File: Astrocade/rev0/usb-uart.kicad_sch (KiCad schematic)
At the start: 13 parts, among them J3 USB-C, U3 CP2102N-A02-GQFN28, U4 UMH3N

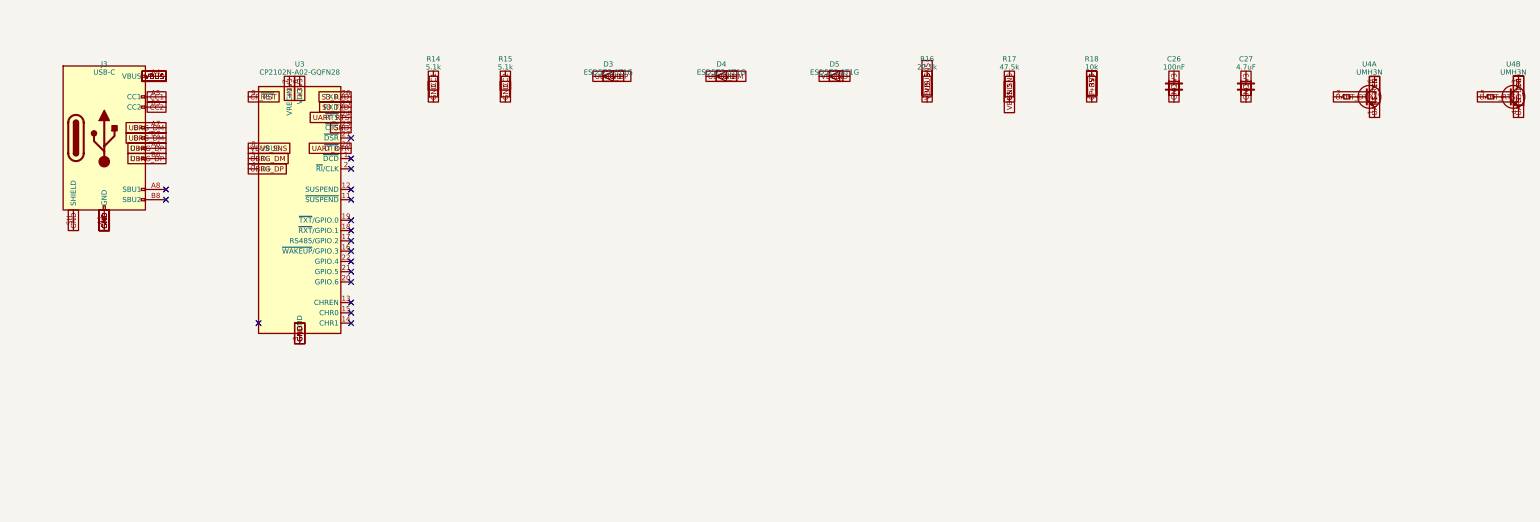
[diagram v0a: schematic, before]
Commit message: Astrocade Rev0: redo on RP2354A + ESP32-S3, 6-layer, fully autorouted
Replaces the unrouted RP2040 + 3x LVC245 draft with an INTV-style board:
RP2354A straight on the 5V bus, ESP32-S3-WROOM-1-N16R8 as its USB host
(PICOBOOT reflash), USB-C/CP2102N, push-push microSD, WS2812B-2020-V6,
RESET/BOOTSEL/EN/BOOT buttons. Same cassette outline, lands and holes.

Everything is generated by tools/ (build_all.sh): design.py -> schematic,
placement + plane fan-out, Raspberry Pi's MIT regulator-corner graft,
Freerouting + A* finisher, netlist-vs-firmware check, JLCPCB BOM/CPL/gerbers.
ERC 0, DRC 0 errors / 0 unconnected / 0 parity, check_nets 174/174.

RUN/BOOTSEL from the S3 are direct 1k links (fnPicoUpdater drives them low;
an NPN driver would invert it). Shell openings come from the placement.

Co-Authored-By: Claude Opus 5.5 (1M context) <noreply@anthropic.com>
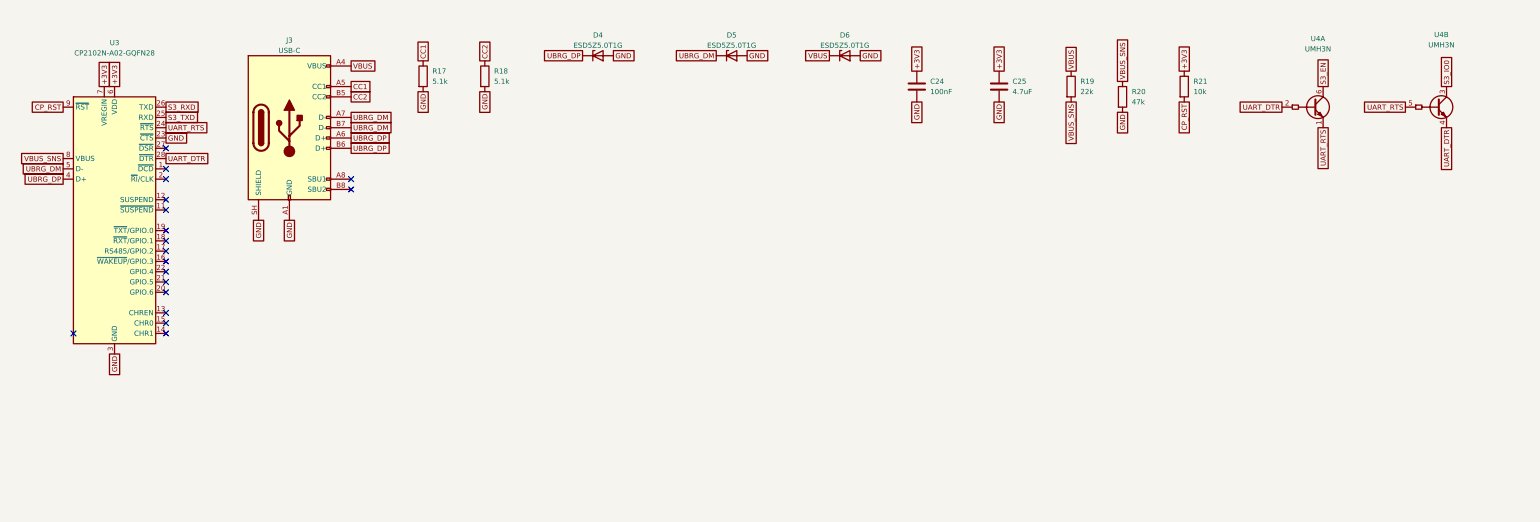
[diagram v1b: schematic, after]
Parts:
- removed C26: 100nF, FujiNet-Astrocade:C_0603_1608Metric, symbol Device:C
- removed C27: 4.7uF, FujiNet-Astrocade:C_0603_1608Metric, symbol Device:C
- removed D3: ESD5Z5.0T1G, FujiNet-Astrocade:D_SOD-523, symbol Diode:ESD5Zxx
- removed R14, R15: 5.1k, FujiNet-Astrocade:R_0603_1608Metric, symbol Device:R
- removed R16: 22.1k, FujiNet-Astrocade:R_0603_1608Metric, symbol Device:R
- added C24: 100nF, FujiNet-Astrocade:C_0603_1608Metric, symbol Device:C
- added C25: 4.7uF, FujiNet-Astrocade:C_0603_1608Metric, symbol Device:C
- added D6: ESD5Z5.0T1G, FujiNet-Astrocade:D_SOD-523, symbol Diode:ESD5Zxx
- added R19: 22k, FujiNet-Astrocade:R_0603_1608Metric, symbol Device:R
- added R20: 47k, FujiNet-Astrocade:R_0603_1608Metric, symbol Device:R
- added R21: 10k, FujiNet-Astrocade:R_0603_1608Metric, symbol Device:R
- D4, D5: LCSC C316061 -> C82044; MPN (none) -> ESD5Z5.0T1G
- J3: LCSC C5178539 -> C165948; MPN HRO TYPE-C-31-M-12 -> TYPE-C-31-M-12
- R17: value 47.5k -> 5.1k; LCSC (none) -> C23186; MPN (none) -> 0603WAF5101T5E
- R18: value 10k -> 5.1k; LCSC (none) -> C23186; MPN (none) -> 0603WAF5101T5E
- U3: LCSC (none) -> C964632
- U4: LCSC C123008 -> C62892; MPN (none) -> UMH3N
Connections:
- net +3V3: now also C24.1, C25.1, R21.1; no longer R18.1
- net CC1: now also R17.1
- net CC2: now also R18.1
- net CP_RST: now also R21.2; no longer R18.2
- net GND: now also R18.2, C24.2, C25.2, D6.2 (A), R20.2
- net UBRG_DM: now also D5.1 (K); no longer D4.1 (K)
- net UBRG_DP: now also D4.1 (K)
- net VBUS: now also D6.1 (K), R19.1; no longer D5.1 (K)
- net VBUS_SNS: now also R19.2, R20.1; no longer R17.1
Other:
- company: (none) -> FujiNet
- title: (none) -> FujiNet Astrocade Rev0 - USB-C, CP2102N programming bridge

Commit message: Astrocade Rev0: audit with kicad-happy + datasheets and redo
Schematic, board and fab outputs regenerated from tools/ after a
datasheet-level audit (docs/design-review-rev0.md).

Design fixes:
- RP2354A on its own AP2112K rail (+3V3_RP): its FT pads take 5.5 V only
  with IOVDD powered (RP2350 DS p.1332); the buck's UVLO + 4 ms soft-start
  left them unpowered while the console drove the bus
- WS2812B-2020-V6 on +5V (datasheet VDD 3.7-5.3 V, not a 3.3 V part)
- VBUS decoupling at the USB-C, activity LED 330R, card-detect polarity
  settled (low = card present), fiducials, RUN/BOOTSEL/rail test pads

Schematic redrawn readably: root block diagram with hierarchical pins,
power symbols, wired clusters and design notes (tools/sch_layout.py);
check_sch_layout.py proves the drawn netlist equals design.py.

Board: 4 layers tried first and did not close; 6 layers, 100% routed,
DRC 0 errors / 0 unconnected / 0 parity. Locked USB-C D+/D- pad ties,
GND stitching kept out of pads, return vias at USB/crystal layer
changes, check_vias.py gate (KiCad re-nets a via inside another net's
pad, so its DRC cannot see it).

Co-Authored-By: Claude Opus 5.5 <noreply@anthropic.com>
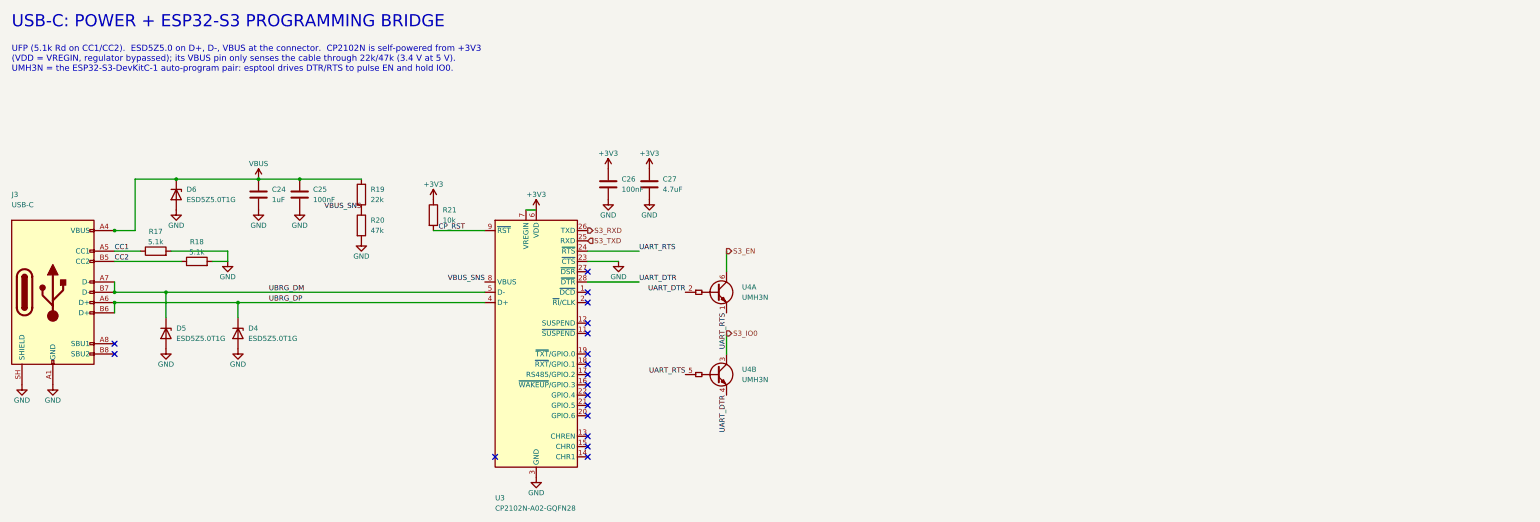
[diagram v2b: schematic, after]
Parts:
- added C26: 100nF, FujiNet-Astrocade:C_0603_1608Metric, symbol Device:C
- added C27: 4.7uF, FujiNet-Astrocade:C_0603_1608Metric, symbol Device:C
- C24: value 100nF -> 1uF; LCSC C14663 -> C15849; MPN CC0603KRX7R9BB104 -> CL10A105KB8NNNC
- C25: value 4.7uF -> 100nF; LCSC C19666 -> C14663; MPN CL10A475KO8NNNC -> CC0603KRX7R9BB104
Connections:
- net +3V3: now also C26.1, C27.1; no longer C24.1, C25.1
- net GND: now also C26.2, C27.2
- net VBUS: now also C24.1, C25.1
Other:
- note added: "UFP (5.1k Rd on CC1/CC2). ESD5Z5.0 on D+, D-, VBUS at the connector. CP2102N is self-powered from +3V3 (VDD = VREGIN, regulator bypassed); its VBUS pin only senses the cable through 22k/47k (3.4 V at 5 V). UMH3N = the ESP32-S3-DevKitC-1 auto-program pair: esptool drives DTR/RTS to pulse EN and hold IO0."
- note added: "USB-C: POWER + ESP32-S3 PROGRAMMING BRIDGE"
- moved on the sheet: C24, C25, D4, D5, D6, J3, R17, R18, R19, R20, R21, U3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
